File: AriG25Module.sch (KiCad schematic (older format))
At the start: 38 parts, among them SW1 BTN, SW2 ~RST, U3 ARIA-G25

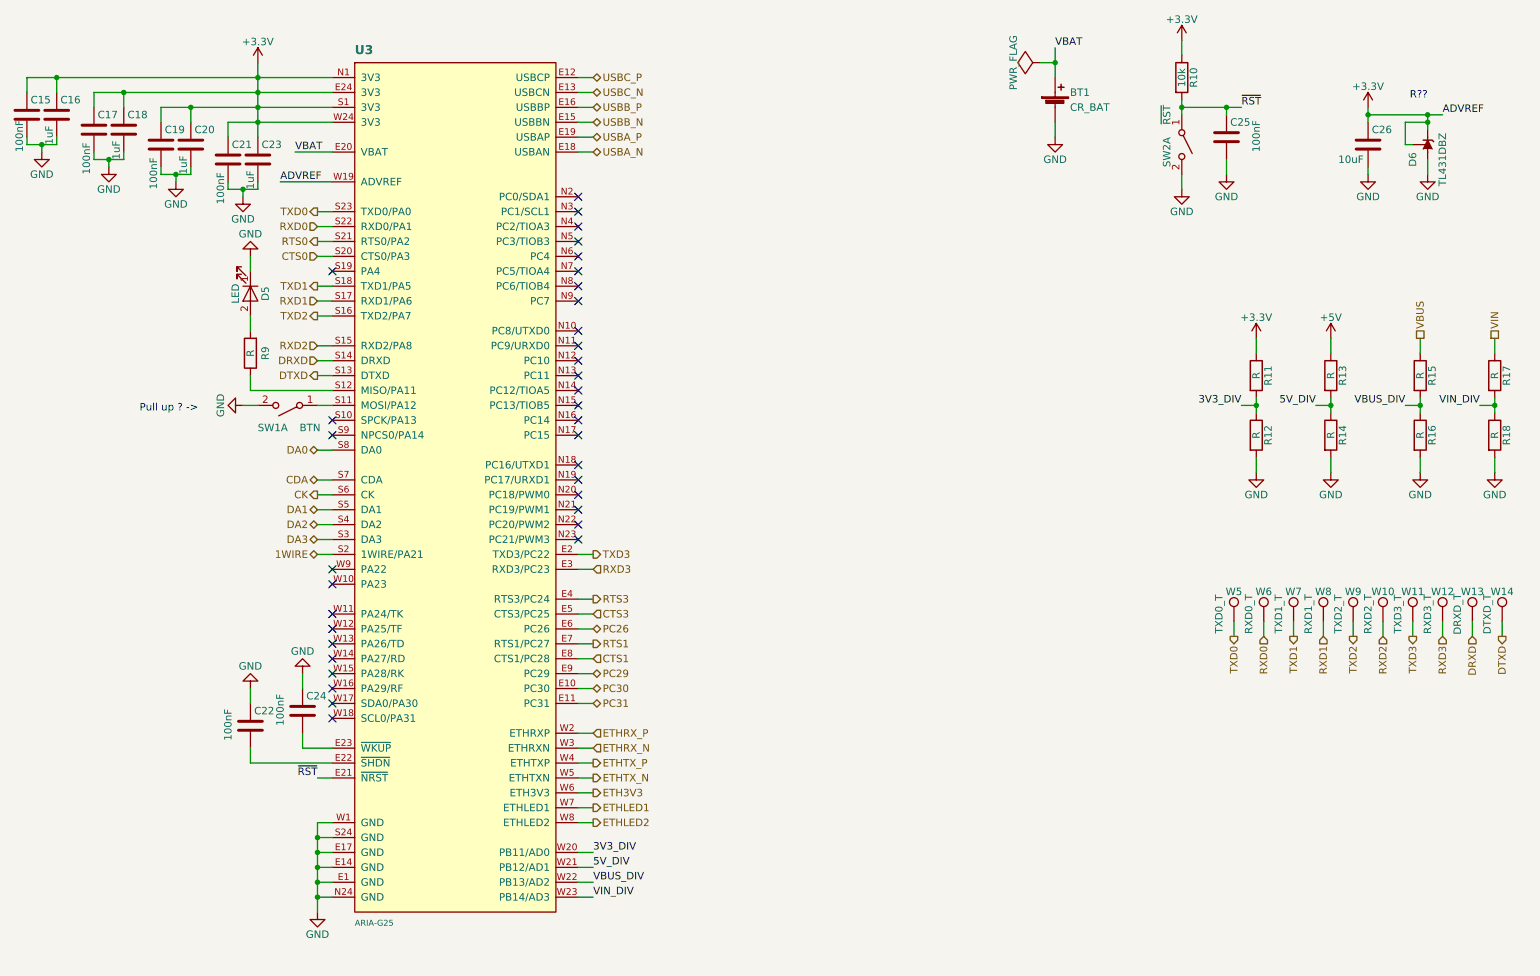
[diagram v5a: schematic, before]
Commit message: Modified board. v1.1 to reflect the schematic change.
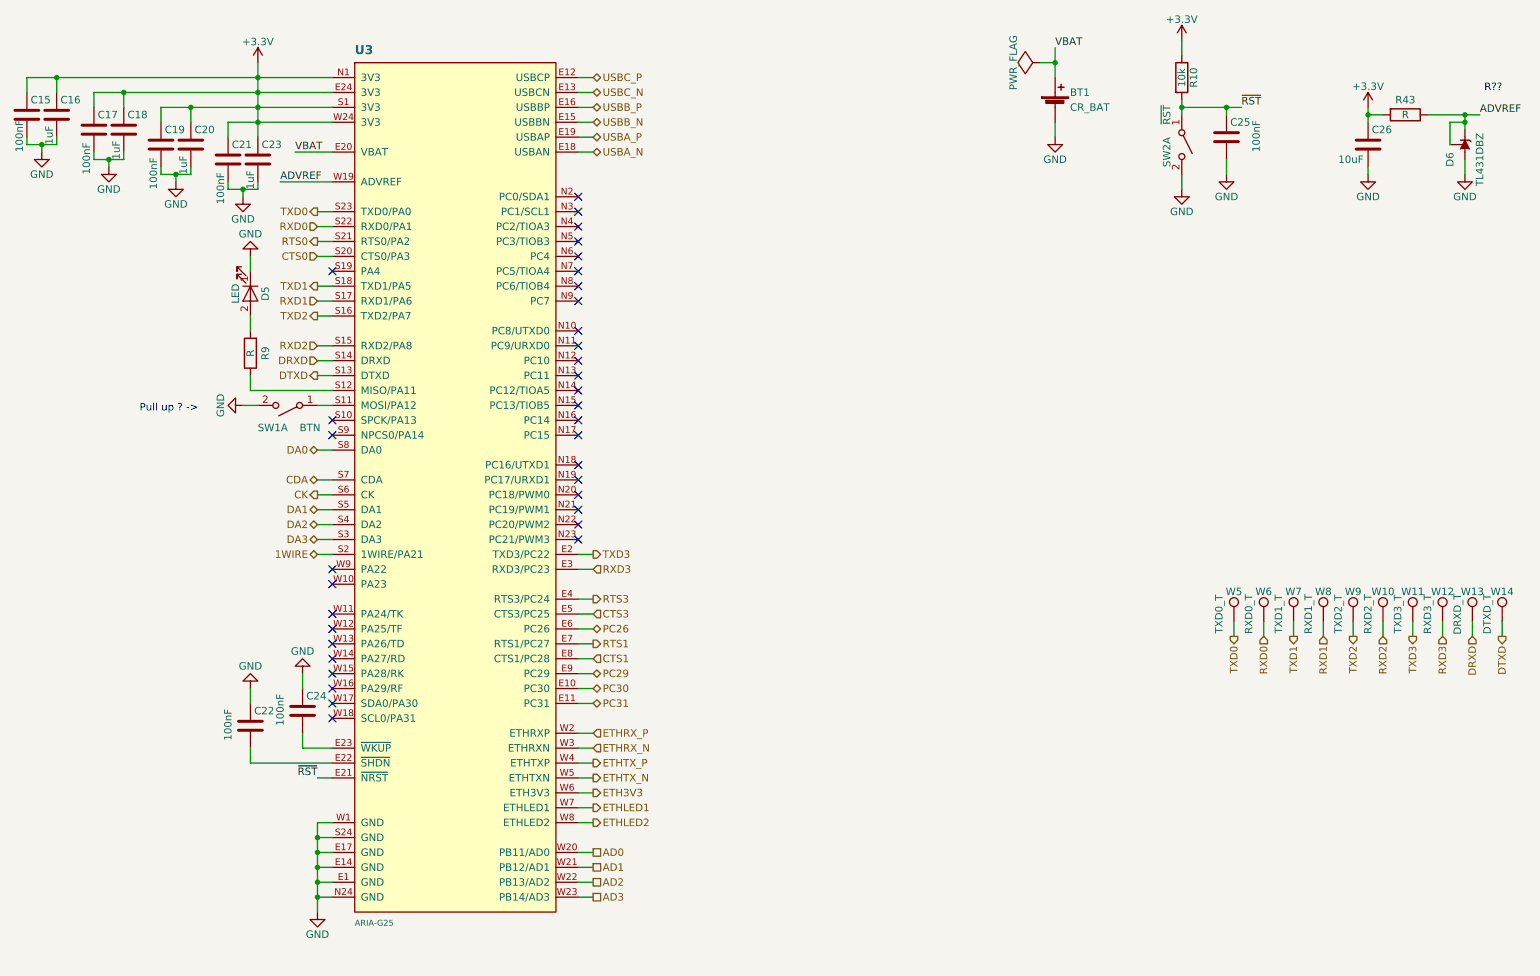
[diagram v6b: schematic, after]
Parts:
- removed R11, R12, R13, R14, R15, R16, R17, R18: R, Resistors_SMD:R_0603_HandSoldering, symbol R
- added R43: R, Resistors_SMD:R_0603_HandSoldering, symbol R
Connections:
- net +3V3: now also R43.2; no longer D6.1 (K), D6.2 (REF), U3.W19 (ADVREF)
- net 3V3_DIV renamed AD0
- net 5V_DIV renamed AD1
- net VBUS_DIV renamed AD2
- net VIN_DIV renamed AD3
- new net ADVREF: D6.1 (K), D6.2 (REF), R43.1, U3.W19 (ADVREF)
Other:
- moved on the sheet: D6
